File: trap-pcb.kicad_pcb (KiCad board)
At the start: 2 copper layers, 150 x 102 mm, 116 parts, among them J1 Conn_01x15, J2 Conn_01x15, M1 Motor_DC, Q1 Q_NMOS_GSD, Q2 Q_NMOS_GSD, Q3 Q_NMOS_GSD, Q4 Q_NMOS_GSD, Q5 Q_NMOS_GSD, Q6 Q_NMOS_GSD, Q7 Q_NMOS_GSD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

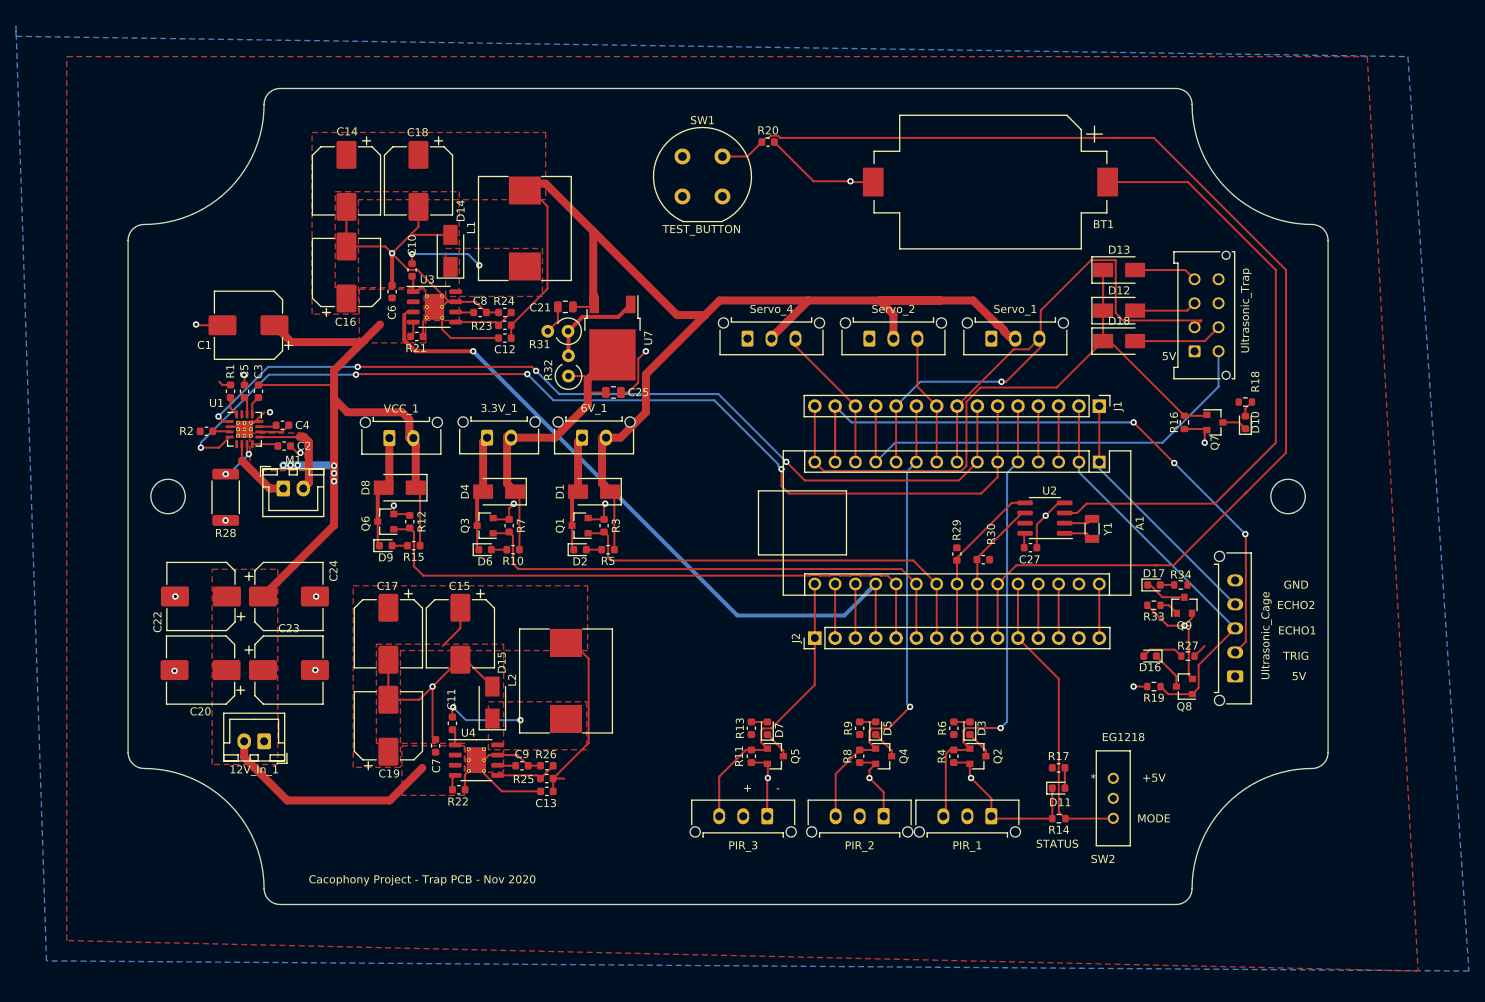
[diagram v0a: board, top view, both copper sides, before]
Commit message: DRC Fixes
Fixed DRC errors. Changed connectors to JST.
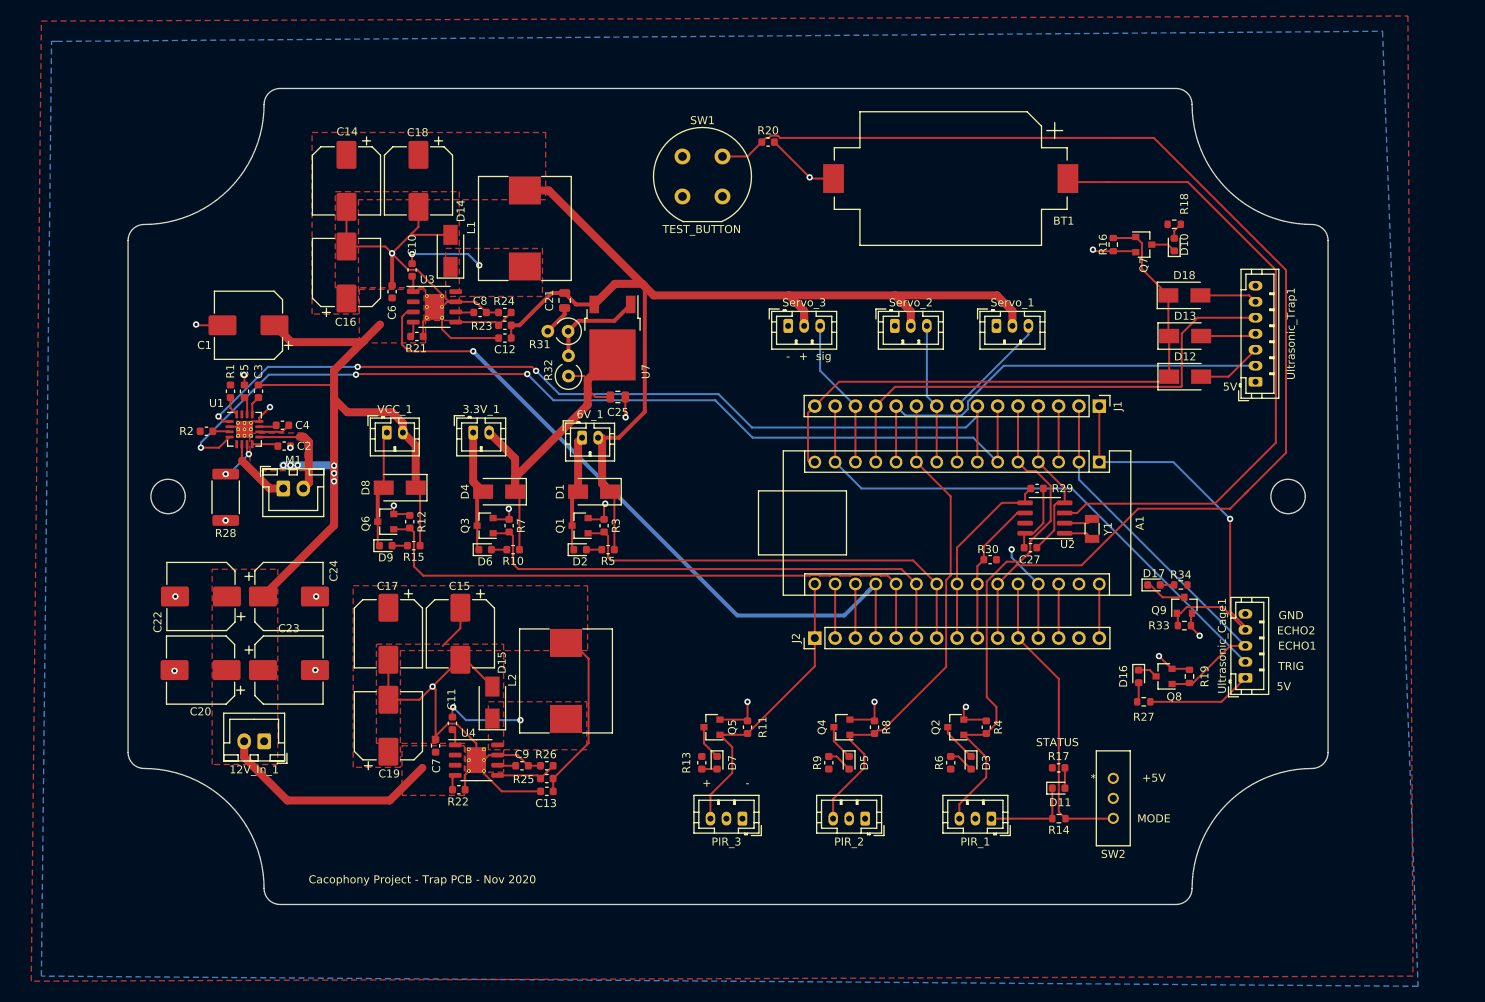
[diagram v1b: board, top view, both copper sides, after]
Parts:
- removed Servo_4: Conn_01x03, Connector_Molex:Molex_Micro-Fit_3.0_43650-0315_1x03_P3.00mm_Vertical
- added Servo_3: Conn_01x03, Connector_JST:JST_PH_B3B-PH-K_1x03_P2.00mm_Vertical, F.Cu at (143.5, 66.7)
- 3.3V_1, 6V_1, VCC_1: value Conn_01x02 -> CONN HEADER VERT 2POS 2MM; footprint Connector_Molex:Molex_Micro-Fit_3.0_43650-0215_1x02_P3.00mm_Vertical -> Connector_JST:JST_PH_B2B-PH-K_1x02_P2.00mm_Vertical
- PIR_1, PIR_2, PIR_3, Servo_1, Servo_2: footprint Connector_Molex:Molex_Micro-Fit_3.0_43650-0315_1x03_P3.00mm_Vertical -> Connector_JST:JST_PH_B3B-PH-K_1x03_P2.00mm_Vertical
- SW2: value EG1218 -> MODE
- Ultrasonic_Cage1: renamed from Ultrasonic_Cage; footprint Connector_Molex:Molex_Micro-Fit_3.0_43650-0515_1x05_P3.00mm_Vertical -> Connector_JST:JST_PH_B5B-PH-K_1x05_P2.00mm_Vertical
- Ultrasonic_Trap1: renamed from Ultrasonic_Trap; footprint Connector_Molex:Molex_Micro-Fit_3.0_43045-0812_2x04_P3.00mm_Vertical -> Connector_JST:JST_PH_B7B-PH-K_1x07_P2.00mm_Vertical
- moved R18 23.9 mm to (191.8, 54.0)
- moved D10 23.9 mm to (191.8, 56.5)
- moved Q7 23.9 mm to (188.0, 56.5)
- moved R16 23.9 mm to (184.2, 56.5)
- moved R29 13.0 mm to (174.6, 87.0), turned to 180 degrees
- moved D12 11.7 mm to (193.1, 73.0)
- moved D13 11.7 mm to (193.1, 67.9)
- moved D18 9.96 mm to (193.0, 62.9)
- moved Q5 8.72 mm to (134.0, 116.8), turned to 180 degrees
- moved Ultrasonic_Trap1 8.52 mm to (201.9, 73.7)
- moved R27 7.95 mm to (188.0, 113.7)
- moved D7 7.63 mm to (134.6, 121.3), turned to 270 degrees
- moved R13 7.55 mm to (132.7, 121.3), turned to 270 degrees
- moved Q4 6.36 mm to (150.2, 116.8), turned to 180 degrees
- moved R9 5.79 mm to (148.6, 121.3)
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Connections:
- net ECHO_CAGE renamed /ECHO_CAGE
- net ECHO_MAIN renamed /ECHO_MAIN
- net TRIGGER_CAGE renamed /TRIGGER_CAGE
- net TRIGGER_F1 renamed /TRIGGER_F1
- net TRIGGER_F2 renamed /TRIGGER_F2
- A1 pad 1: ECHO_CAGE2 -> /ECHO_CAGE2
- J1 pad 1: ECHO_CAGE2 -> /ECHO_CAGE2
- Q9 pad 1: Net-(Q9-Pad1) -> /ECHO_CAGE2
- R33 pad 1: Net-(Q9-Pad1) -> /ECHO_CAGE2
- Ultrasonic_Cage1 pad 4: ECHO_CAGE2 -> /ECHO_CAGE2
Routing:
- net /ECHO_CAGE2: track 0.00 -> 52.8 mm, vias 0 -> 1
- net ECHO_CAGE2: track 31.8 -> 0.00 mm
- net +6V: track 162.7 -> 139.2 mm
- net +5V: track 41.8 -> 62.7 mm, vias 0 -> 1
- net /TRIGGER_CAGE: track 86.5 -> 68.6 mm, vias 3 -> 0
- net GND: track 228.3 -> 214.0 mm, vias 23 -> 22
- net /TRIGGER_F1: track 63.6 -> 55.5 mm, vias 1 -> 0
- net +3V3: track 39.1 -> 45.2 mm
- net /Motor_Enable: track 125.2 -> 119.5 mm, vias 4 -> 3
- net /PIR_1: track 59.6 -> 64.8 mm, vias 1 -> 0
- net /ECHO_MAIN: track 80.7 -> 75.8 mm
- net /TRIGGER_F2: track 58.2 -> 62.9 mm
- net /PIR_2: track 58.7 -> 63.0 mm, vias 1 -> 0
- net Net-(BT1-Pad1): track 78.6 -> 82.6 mm
- net Net-(D18-Pad2): track 11.1 -> 7.22 mm
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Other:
- board text added: "sig"

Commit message: Updated JLC and DigiKey parts
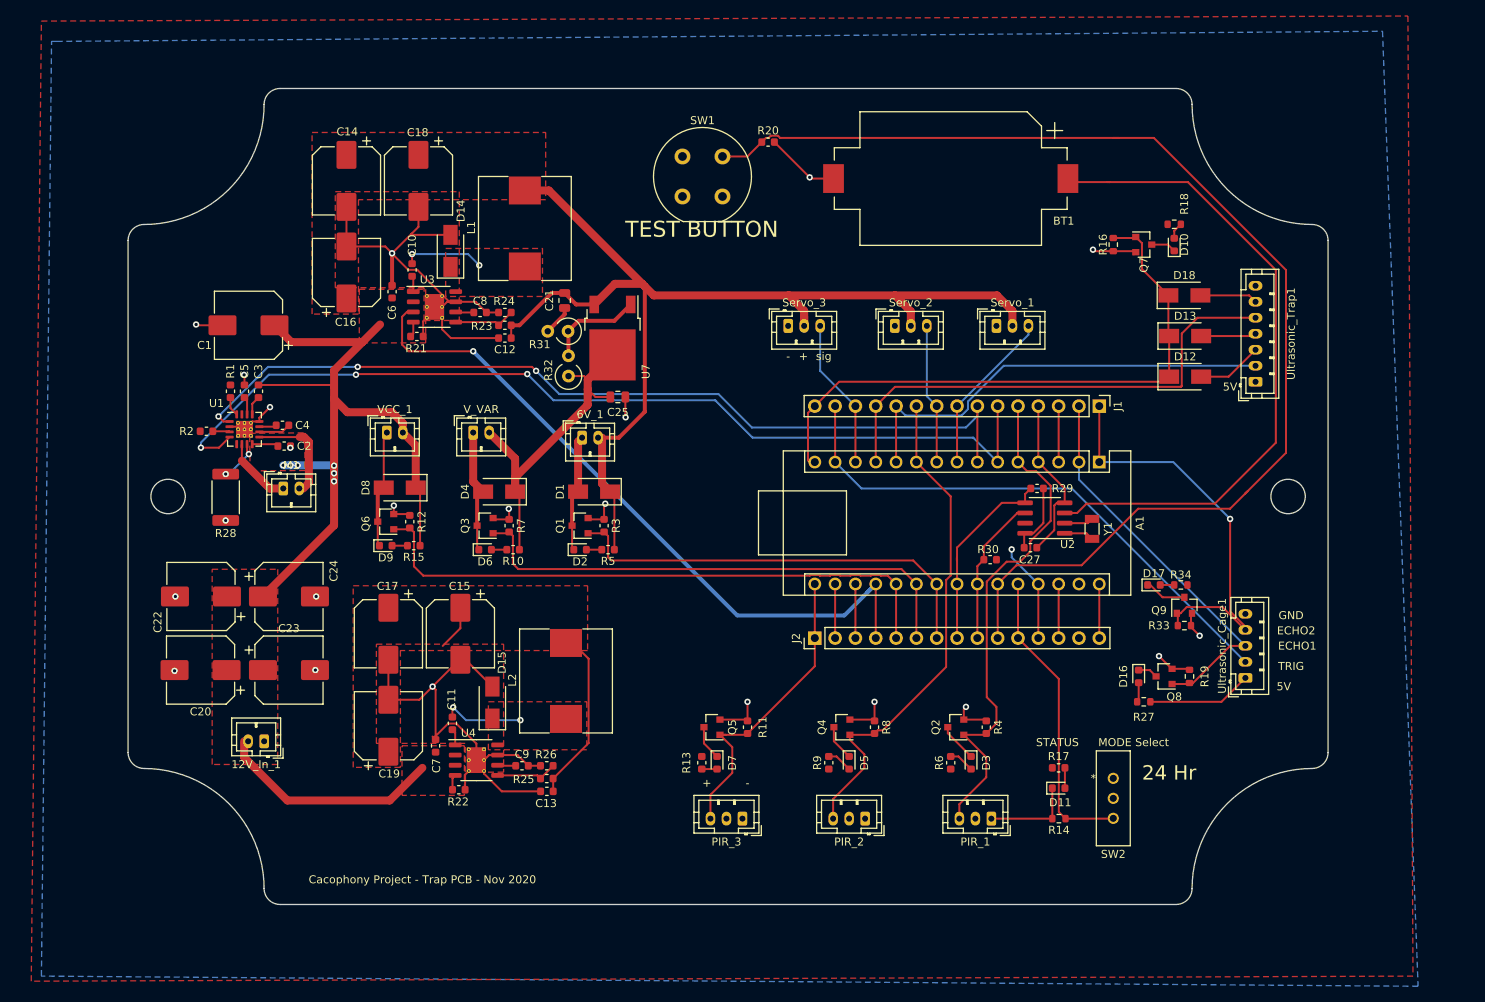
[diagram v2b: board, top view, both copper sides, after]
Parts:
- 12V_In_1, M1: footprint Connector_JST:JST_XH_B2B-XH-A_1x02_P2.50mm_Vertical -> Connector_JST:JST_PH_B2B-PH-K_1x02_P2.00mm_Vertical
- SW2: value MODE -> EG1218
- renumbered 3.3V_1 to V_VAR
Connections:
- net +3V3 renamed VDD
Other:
- board text added: "24 Hr"
- board text added: "MODE Select"
- board text added: "TEST BUTTON"
- board text removed: "+5V"
- board text removed: "MODE"
- board text removed: "TEST_BUTTON"
